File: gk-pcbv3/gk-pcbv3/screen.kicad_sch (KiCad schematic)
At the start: 10 parts, among them J3 Conn_02x15_Counter_Clockwise, U11 ULN2003A

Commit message: v3 board
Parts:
- removed J3: Conn_02x15_Counter_Clockwise, symbol Connector_Generic:Conn_02x15_Counter_Clockwise
- added C30: 22u, Capacitor_SMD:C_0805_2012Metric, symbol Device:C
- added C31: 2.2u, Capacitor_SMD:C_0805_2012Metric, symbol Device:C
- added C32, C5, C6: 100n, Capacitor_SMD:C_0603_1608Metric, symbol Device:C
- added D4: D, Diode_SMD:D_SOD-128, symbol Device:D
- added J10: TE 1-1734839-0, Connector_FFC-FPC:TE_1-1734839-0_1x10-1MP_P0.5mm_Horizontal, symbol Connector_Generic:Conn_01x10
- added J3: Conn_02x27_Top_Bottom, amphenol:AMPHENOL_F32Q-1A7H1-11054, symbol Connector_Generic:Conn_02x27_Top_Bottom
- added L1: 10u, Inductor_SMD:L_7.3x7.3_H3.5, symbol Device:L
- added R4: 100k, Resistor_SMD:R_0603_1608Metric, symbol Device:R
- added R5: 20R, Resistor_SMD:R_2512_6332Metric, symbol Device:R
- added R52: 10k, Resistor_SMD:R_0603_1608Metric, symbol Device:R
- added TP10, TP11, TP9: TestPoint, TestPoint:TestPoint_Pad_D1.0mm, symbol Connector:TestPoint
- added U13: TMUX1237, Package_TO_SOT_SMD:SOT-363_SC-70-6, symbol gk-syms:TMUX1237
- added U22: PT4110E89E, Package_TO_SOT_SMD:SOT-89-5, symbol gk-syms:PT4110
- added U3: ICS570BLF, Package_SO:SO-8_3.9x4.9mm_P1.27mm, symbol gk-syms:ICS570BLF
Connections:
- net GND: now also C30.2, C31.2, C32.2, C5.2, C6.2, J10.1 (Pin_1), J3.53 (Pin_53), J3.54 (Pin_54), R4.2, R5.2, R52.2, U13.5 (GND), U22.2 (GND), U3.3 (GND), U3.6 (S0)
- net VCC: now also C32.1, C5.1, C6.1, J10.2 (Pin_2), J3.41 (Pin_41), J3.42 (Pin_42), U13.2 (VCC), U3.1 (S1), U3.2 (VCC)
- new net: J3.1 (Pin_1), J3.2 (Pin_2), R5.1, U22.4 (FB)
- new net: D4.2 (A), L1.2, U22.5 (SW)
- new net: TP10.1, U13.1 (S2), U3.7 (CLK)
- new net: U3.5 (FBIN), U3.8 (CLK/2)
- new net: C31.1, D4.1 (K), J3.3 (Pin_3), J3.4 (Pin_4)
- new net +5V: C30.1, L1.1, U22.1 (IN)
- new net CTP_INT: J10.9 (Pin_9)
- new net CTP_NRESET: J10.7 (Pin_7), R52.1
- new net I2C2_SCL: J10.3 (Pin_3)
- new net I2C2_SDA: J10.5 (Pin_5)
- new net LCD_CS: J3.9 (Pin_9)
- new net LCD_RESET: J3.8 (Pin_8)
- new net LCD_SCL: J3.10 (Pin_10)
- new net LCD_SDI: J3.11 (Pin_11)
- new net LCD_SDO: J3.7 (Pin_7)
- new net LED_BACKLIGHT_PWM: R4.1, U22.3 (EN)
- new net LTDC_B0: J3.12 (Pin_12)
- new net LTDC_B1: J3.13 (Pin_13)
- new net LTDC_B2: J3.14 (Pin_14)
- new net LTDC_B3: J3.15 (Pin_15)
- new net LTDC_B4: J3.16 (Pin_16)
- new net LTDC_B5: J3.17 (Pin_17)
- new net LTDC_B6: J3.18 (Pin_18)
- new net LTDC_B7: J3.19 (Pin_19)
- new net LTDC_CLK: TP9.1, U13.3 (S1), U3.4 (ICLK)
- new net LTDC_CLK_OUT: J3.38 (Pin_38), TP11.1, U13.4 (D)
- new net LTDC_CLK_SELECT: U13.6 (SEL)
- new net LTDC_DE: J3.52 (Pin_52)
- new net LTDC_G0: J3.20 (Pin_20)
- new net LTDC_G1: J3.21 (Pin_21)
- new net LTDC_G2: J3.22 (Pin_22)
- new net LTDC_G3: J3.23 (Pin_23)
- new net LTDC_G4: J3.24 (Pin_24)
- new net LTDC_G5: J3.25 (Pin_25)
- new net LTDC_G6: J3.26 (Pin_26)
- new net LTDC_G7: J3.27 (Pin_27)
- new net LTDC_HSYNC: J3.36 (Pin_36)
- new net LTDC_R0: J3.28 (Pin_28)
- new net LTDC_R1: J3.29 (Pin_29)
- new net LTDC_R2: J3.30 (Pin_30)
- new net LTDC_R3: J3.31 (Pin_31)
- new net LTDC_R4: J3.32 (Pin_32)
- new net LTDC_R5: J3.33 (Pin_33)
- new net LTDC_R6: J3.34 (Pin_34)
- new net LTDC_R7: J3.35 (Pin_35)
- new net LTDC_VSYNC: J3.37 (Pin_37)
- no-connect marks 16 -> 18
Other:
- note added: "Half width clock (400x500x60 = 12 MHz) to full width (24 MHz)"
- note added: "Pin 1 near edge of board"
- note added: "Touchscreen is Waveshare 3.5 DPI removed from carrier board LLCD is ER-TFT035-7 compatible pinout Touch is GT911"
- note removed: "TODO review for new touchscreen"

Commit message: more v3 changes
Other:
- note added: "Touchscreen is Waveshare 3.5 DPI removed from carrier board LCD is ER-TFT035-7 compatible pinout Touch is GT911"
- note removed: "Touchscreen is Waveshare 3.5 DPI removed from carrier board LLCD is ER-TFT035-7 compatible pinout Touch is GT911"
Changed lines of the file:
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@@
 		)
 	)
-	(text "Touchscreen is Waveshare 3.5 DPI removed from carrier board\nLLCD is ER-TFT035-7 compatible pinout\nTouch is GT911"
+	(text "Touchscreen is Waveshare 3.5 DPI removed from carrier board\nLCD is ER-TFT035-7 compatible pinout\nTouch is GT911"
 		(exclude_from_sim no)
 		(at 117.602 21.082 0)

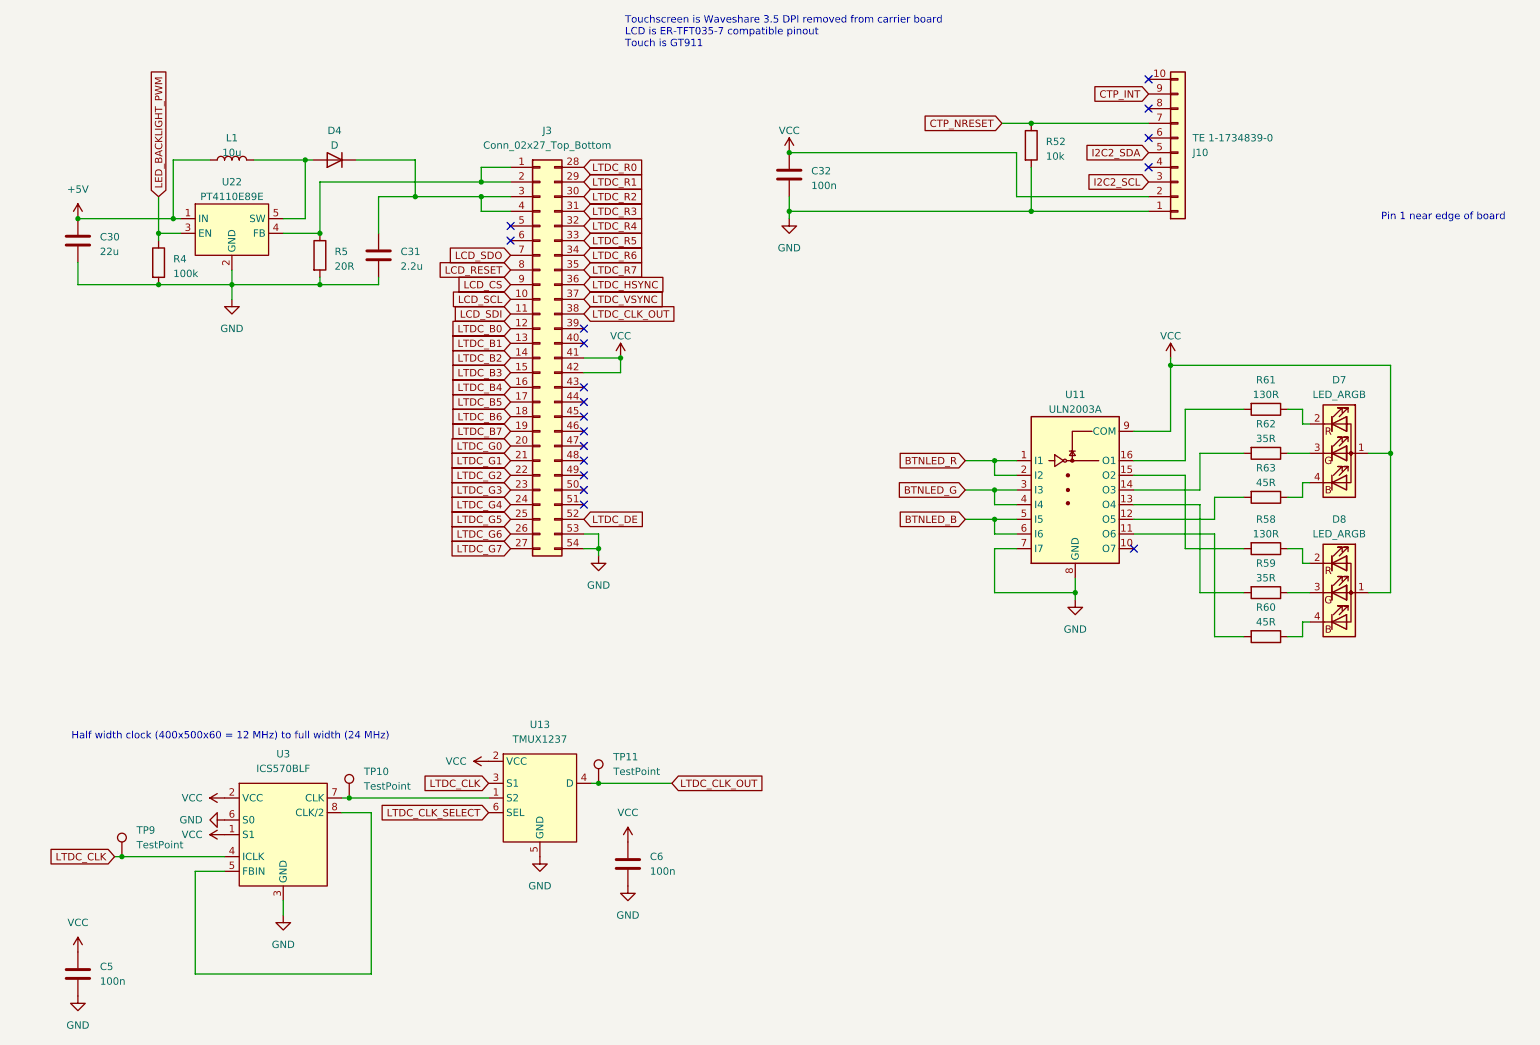
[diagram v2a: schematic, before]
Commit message: redesign for better signal integrity
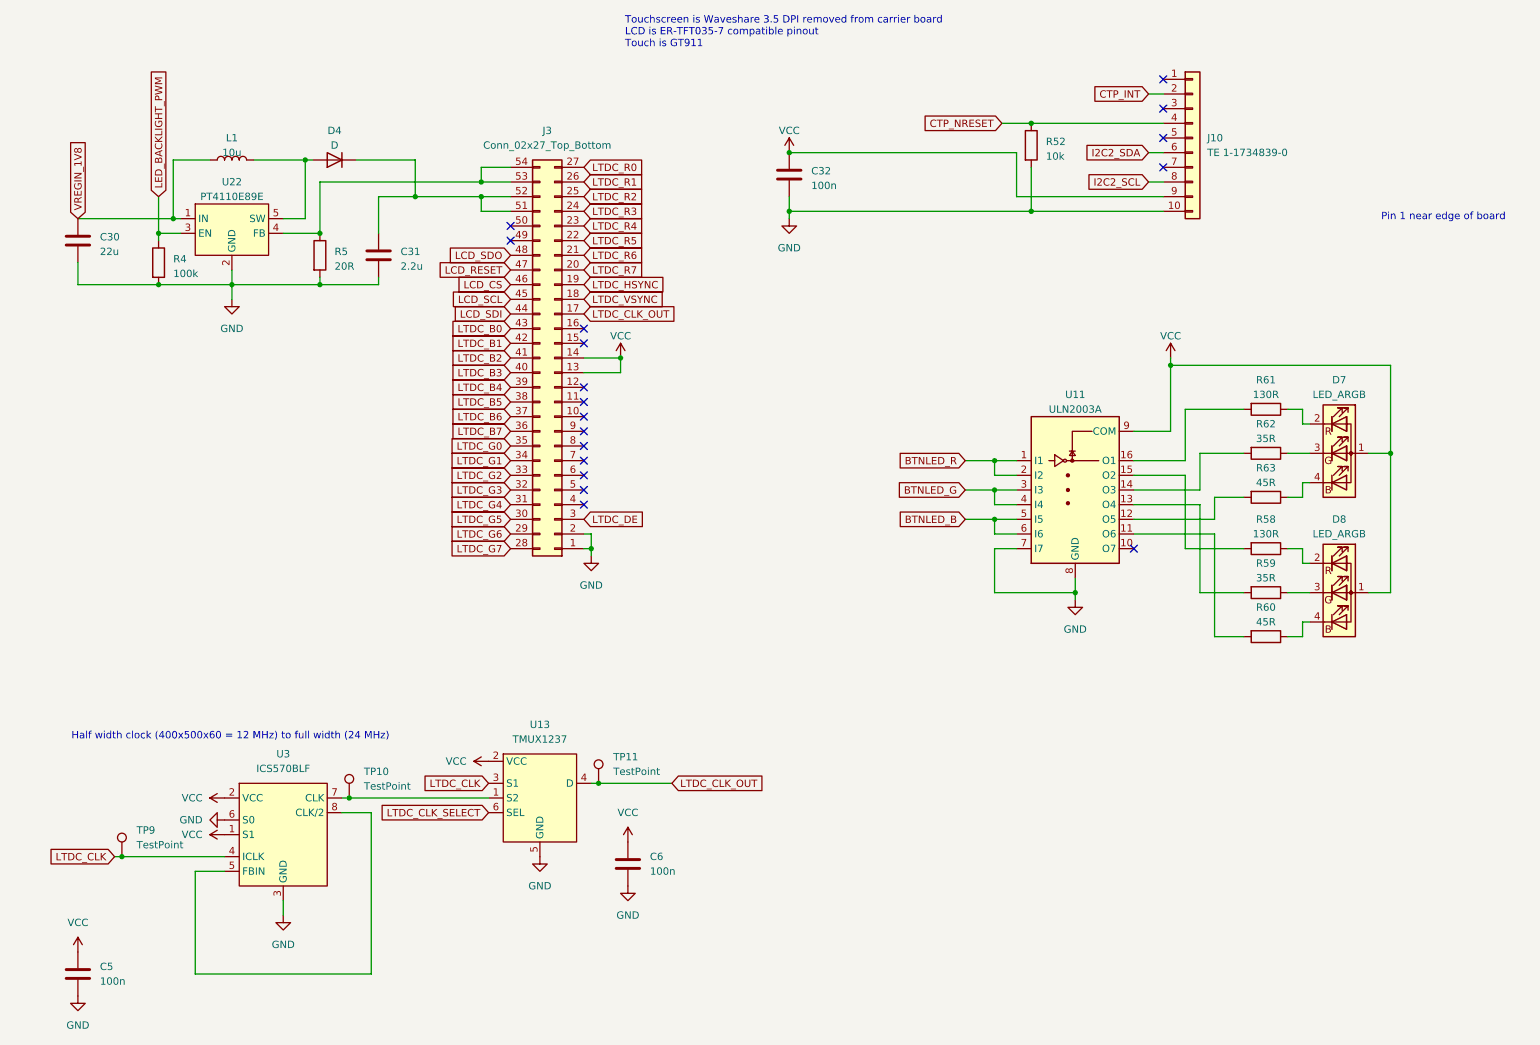
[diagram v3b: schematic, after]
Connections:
- net CTP_INT: now also J10.2 (Pin_2); no longer J10.9 (Pin_9)
- net CTP_NRESET: now also J10.4 (Pin_4); no longer J10.7 (Pin_7)
- net GND: now also J10.10 (Pin_10), J3.1 (Pin_1), J3.2 (Pin_2); no longer J10.1 (Pin_1), J3.53 (Pin_53), J3.54 (Pin_54)
- net I2C2_SCL: now also J10.8 (Pin_8); no longer J10.3 (Pin_3)
- net I2C2_SDA: now also J10.6 (Pin_6); no longer J10.5 (Pin_5)
- net LCD_CS: now also J3.46 (Pin_46); no longer J3.9 (Pin_9)
- net LCD_RESET: now also J3.47 (Pin_47); no longer J3.8 (Pin_8)
- net LCD_SCL: now also J3.45 (Pin_45); no longer J3.10 (Pin_10)
- net LCD_SDI: now also J3.44 (Pin_44); no longer J3.11 (Pin_11)
- net LCD_SDO: now also J3.48 (Pin_48); no longer J3.7 (Pin_7)
- net LTDC_B0: now also J3.43 (Pin_43); no longer J3.12 (Pin_12)
- net LTDC_B1: now also J3.42 (Pin_42); no longer J3.13 (Pin_13)
- net LTDC_B2: now also J3.41 (Pin_41); no longer J3.14 (Pin_14)
- net LTDC_B3: now also J3.40 (Pin_40); no longer J3.15 (Pin_15)
- net LTDC_B4: now also J3.39 (Pin_39); no longer J3.16 (Pin_16)
- net LTDC_B5: now also J3.38 (Pin_38); no longer J3.17 (Pin_17)
- net LTDC_B6: now also J3.37 (Pin_37); no longer J3.18 (Pin_18)
- net LTDC_B7: now also J3.36 (Pin_36); no longer J3.19 (Pin_19)
- net LTDC_CLK_OUT: now also J3.17 (Pin_17); no longer J3.38 (Pin_38)
- net LTDC_DE: now also J3.3 (Pin_3); no longer J3.52 (Pin_52)
- net LTDC_G0: now also J3.35 (Pin_35); no longer J3.20 (Pin_20)
- net LTDC_G1: now also J3.34 (Pin_34); no longer J3.21 (Pin_21)
- net LTDC_G2: now also J3.33 (Pin_33); no longer J3.22 (Pin_22)
- net LTDC_G3: now also J3.32 (Pin_32); no longer J3.23 (Pin_23)
- net LTDC_G4: now also J3.31 (Pin_31); no longer J3.24 (Pin_24)
- net LTDC_G5: now also J3.30 (Pin_30); no longer J3.25 (Pin_25)
- net LTDC_G6: now also J3.29 (Pin_29); no longer J3.26 (Pin_26)
- net LTDC_G7: now also J3.28 (Pin_28); no longer J3.27 (Pin_27)
- net LTDC_HSYNC: now also J3.19 (Pin_19); no longer J3.36 (Pin_36)
- net LTDC_R0: now also J3.27 (Pin_27); no longer J3.28 (Pin_28)
- net LTDC_R1: now also J3.26 (Pin_26); no longer J3.29 (Pin_29)
- net LTDC_R2: now also J3.25 (Pin_25); no longer J3.30 (Pin_30)
- net LTDC_R3: now also J3.24 (Pin_24); no longer J3.31 (Pin_31)
- net LTDC_R4: now also J3.23 (Pin_23); no longer J3.32 (Pin_32)
- net LTDC_R5: now also J3.22 (Pin_22); no longer J3.33 (Pin_33)
- net LTDC_R6: now also J3.21 (Pin_21); no longer J3.34 (Pin_34)
- net LTDC_R7: now also J3.20 (Pin_20); no longer J3.35 (Pin_35)
- net LTDC_VSYNC: now also J3.18 (Pin_18); no longer J3.37 (Pin_37)
- net VCC: now also J10.9 (Pin_9), J3.13 (Pin_13), J3.14 (Pin_14); no longer J10.2 (Pin_2), J3.41 (Pin_41), J3.42 (Pin_42)
- net at R5.1, U22.4 (FB): now also J3.53 (Pin_53), J3.54 (Pin_54); no longer J3.1 (Pin_1), J3.2 (Pin_2)
- net at C31.1, D4.1 (K): now also J3.51 (Pin_51), J3.52 (Pin_52); no longer J3.3 (Pin_3), J3.4 (Pin_4)
- net +5V renamed VREGIN_1V8
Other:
- moved on the sheet: J10, J3

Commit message: update schematics for new vreg design
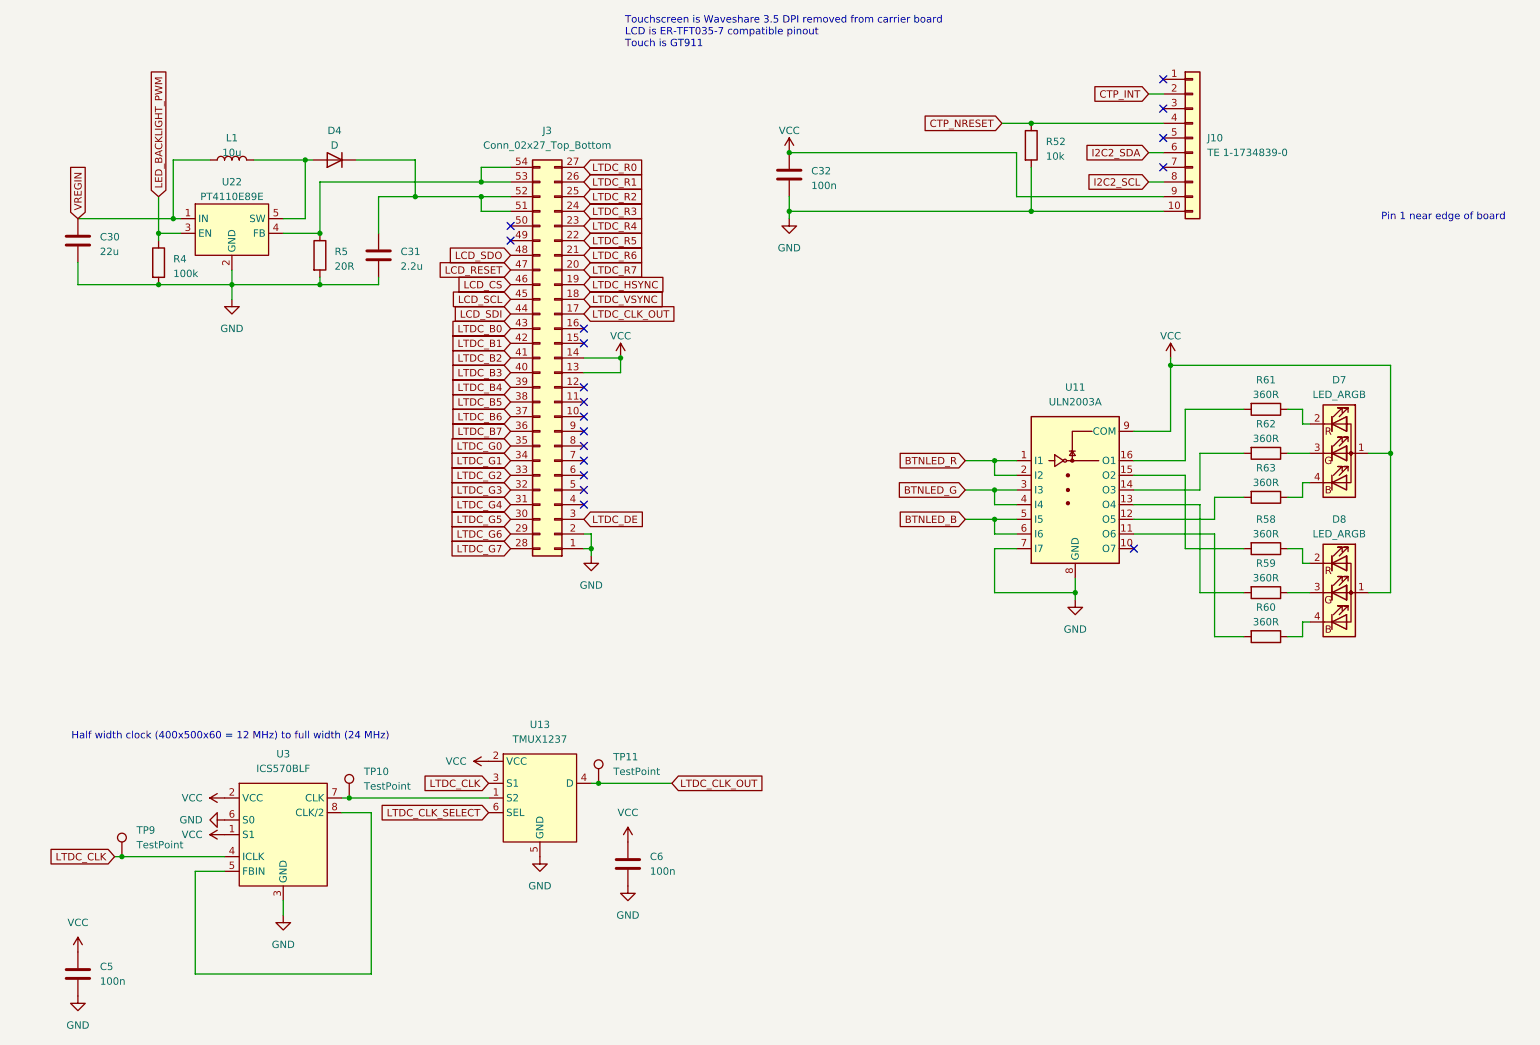
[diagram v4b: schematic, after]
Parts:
- R58, R61: value 130R -> 360R
- R59, R62: value 35R -> 360R
- R60, R63: value 45R -> 360R
- U11: footprint Package_SO:SOIC-16W_5.3x10.2mm_P1.27mm -> Package_SO:SOIC-16_3.9x9.9mm_P1.27mm
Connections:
- net VREGIN_1V8 renamed VREGIN
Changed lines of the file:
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@@
 		)
 	)
-	(global_label "VREGIN_1V8"
+	(global_label "VREGIN"
 		(shape input)
 		(at 22.86 53.34 90)
@@
 		)
 		(property "Intersheetrefs" "${INTERSHEET_REFS}"
-			(at 22.86 39.1667 90)
+			(at 22.86 43.6419 90)
 			(effects
 				(font
@@
 			)
 		)
-		(property "Value" "35R"
+		(property "Value" "360R"
 			(at 228.6 115.57 90)
 			(effects
@@
 			)
 		)
-		(property "Value" "45R"
+		(property "Value" "360R"
 			(at 228.6 99.06 90)
 			(effects
@@
 			)
 		)
-		(property "Value" "45R"
+		(property "Value" "360R"
 			(at 228.6 123.19 90)
 			(effects
@@
 			)
 		)
-		(property "Value" "130R"
+		(property "Value" "360R"
 			(at 228.6 83.82 90)
 			(effects
@@
 		(fields_autoplaced yes)
 		(property "Reference" "U11"
-			(at 195.58 83.82 0)
+			(at 195.58 82.55 0)
 			(effects
 				(font
@@
 		)
 		(property "Value" "ULN2003A"
-			(at 195.58 86.36 0)
+			(at 195.58 85.09 0)
 			(effects
 				(font
@@
 			)
 		)
-		(property "Footprint" "Package_SO:SOIC-16W_5.3x10.2mm_P1.27mm"
+		(property "Footprint" "Package_SO:SOIC-16_3.9x9.9mm_P1.27mm"
 			(at 196.85 114.3 0)
 			(effects
@@
 			)
 		)
-		(property "Value" "35R"
+		(property "Value" "360R"
 			(at 228.6 91.44 90)
 			(effects
@@
 			)
 		)
-		(property "Value" "130R"
+		(property "Value" "360R"
 			(at 228.6 107.95 90)
 			(effects
